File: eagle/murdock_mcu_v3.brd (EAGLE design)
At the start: 47 x 31.8 mm, 32 parts, among them IC1 MPU-9150, IC2 LT1763CS8-3.3, IC3 STM32F4XX_64, IC4 BMP085, Q2 PFET, U1 USD-SOCKETNEW, X1 USBSMD, X2 MURDOCK_STACK

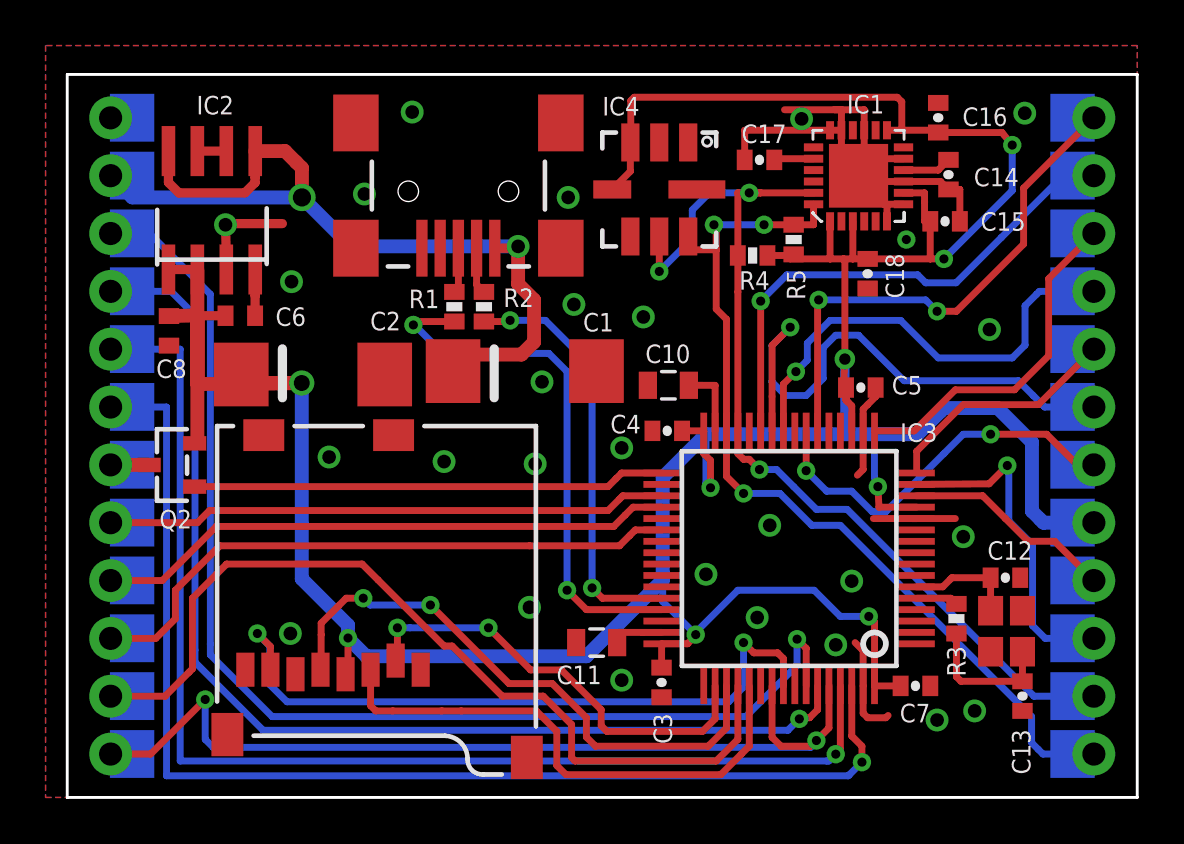
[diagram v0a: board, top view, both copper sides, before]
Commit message: usb placement & smaller tantal
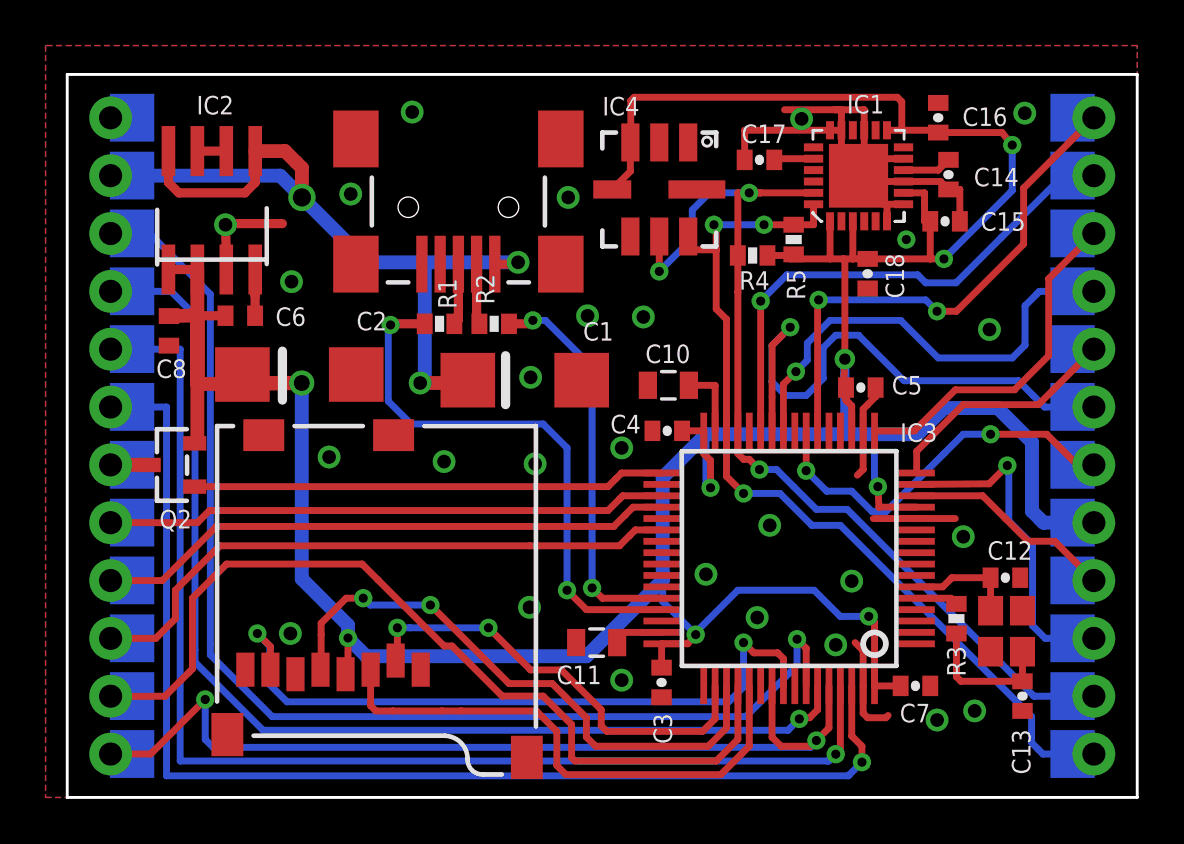
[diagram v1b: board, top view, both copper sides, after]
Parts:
- C1, C2: device rcl:SMC_D -> rcl:SMC_C
- moved R1 0.99 mm to (16.4, 20.8), turned to 0 degrees
- moved R2 0.87 mm to (18.8, 20.8), turned to 180 degrees
- moved X1 0.70 mm to (17.2, 25.9)
- moved C2 0.60 mm to (10.2, 18.6)
- moved C1 0.40 mm to (20.1, 18.3)
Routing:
- net A11: track 18.6 -> 17.5 mm
- net A12: track 23.6 -> 24.4 mm
- net +5V: track 39.4 -> 38.6 mm, vias 2 -> 3
- net N$2: track 1.99 -> 2.69 mm
- net N$1: track 2.05 -> 2.67 mm

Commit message: bootloader robustness
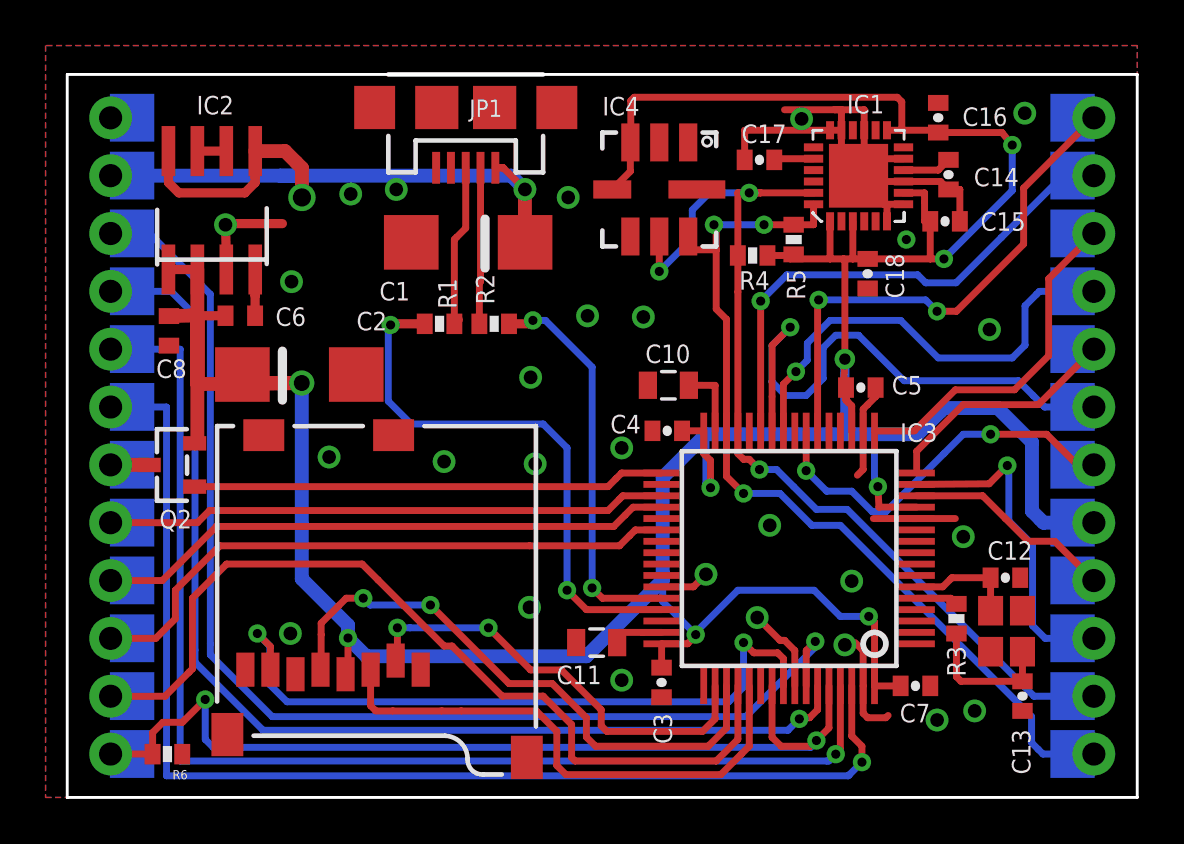
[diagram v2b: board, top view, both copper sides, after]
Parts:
- removed X1: USBSMD, SparkFun-Connectors:USB-MINIB
- added JP1: USB-MICROB, SparkFun-Connectors:USB-MICROB
- added R6: 15k, SparkFun:0402-RES
- moved C1 6.55 mm to (17.6, 24.4), turned to 180 degrees
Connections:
- net +5V: now also JP1.VBUS; no longer X1.VBUS
- net GND: now also IC3.43, IC3.57, JP1.GND, JP1.MT1, JP1.MT2, R6.1; no longer X1.GND
- net N$1: now also JP1.D-; no longer X1.D-
- net N$2: now also JP1.D+; no longer X1.D+
- net SW1: now also R6.2
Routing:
- net GND: track 45.0 -> 51.0 mm
- net N$2: track 2.69 -> 7.31 mm
- net N$1: track 2.67 -> 7.04 mm
- net +5V: track 38.6 -> 35.3 mm, vias 3 -> 2
- net SW1: track 41.1 -> 41.7 mm
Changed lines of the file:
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@@
 <wire x1="3.95" y1="23.615" x2="3.95" y2="23.405" width="0.2" layer="21"/>
 <wire x1="3.95" y1="23.615" x2="8.76" y2="23.625" width="0.2" layer="21"/>
-<wire x1="19.25" y1="17.25" x2="19.25" y2="19.4" width="0.4064" layer="21"/>
+<wire x1="18.35" y1="23.25" x2="18.35" y2="25.4" width="0.4064" layer="21"/>
 <wire x1="9.45" y1="17.45" x2="9.45" y2="19.6" width="0.4064" layer="21"/>
 <text x="18.35" y="18.9" size="1.4224" layer="22" font="vector" ratio="10" rot="MR0">MURDOCK</text>
@@
 <attribute name="VALUE" x="29.7975" y="6.6875" size="1.27" layer="27" rot="R90"/>
 </element>
-<element name="X1" library="SparkFun-Connectors" package="USB-MINIB" value="USBSMD" x="17.1775" y="25.92" smashed="yes" rot="R270">
-<attribute name="VALUE" x="17.1775" y="29.73" size="0.4064" layer="27" rot="R270"/>
-</element>
 <element name="U1" library="SparkFun-Connectors" package="MICRO-SD-SOCKET-PP" value="USD-SOCKETNEW" x="6.5825" y="16.31" smashed="yes" rot="R180">
 <attribute name="VALUE" x="15.4725" y="11.23" size="0.8128" layer="27" rot="R180"/>
@@
 <attribute name="VALUE" x="4.7725" y="19.155" size="0.6096" layer="27" font="vector" ratio="10" rot="R90"/>
 </element>
-<element name="C1" library="rcl" package="SMC_C" value="47µF/10V" x="20.0925" y="18.3225" smashed="yes">
-<attribute name="NAME" x="22.6525" y="20.0625" size="0.8128" layer="25" font="vector" ratio="10"/>
-<attribute name="VALUE" x="17.5525" y="14.5125" size="1.016" layer="27"/>
+<element name="C1" library="rcl" package="SMC_C" value="47µF/10V" x="17.6075" y="24.3775" smashed="yes" rot="R180">
+<attribute name="NAME" x="15.0475" y="22.6375" size="0.8128" layer="25" font="vector" ratio="10" rot="R180"/>
+<attribute name="VALUE" x="20.1475" y="28.1875" size="1.016" layer="27" rot="R180"/>
 </element>
 <element name="C2" library="rcl" package="SMC_C" value="100µF/6V" x="10.1925" y="18.5725" smashed="yes">
@@
 <element name="U$1" library="seb" package="C3D2_LOGO_SMALL" value="" x="17.1" y="22.55" rot="MR0"/>
 <element name="IC4" library="SparkFun-Sensors" package="BMP085" value="BMP085" x="26" y="26.7" smashed="yes" rot="R270"/>
+<element name="JP1" library="SparkFun-Connectors" package="USB-MICROB" value="USB-MICROB" x="17.5" y="30.3" rot="R180">
+<attribute name="PROD_ID" value="CONN-09505" x="17.5" y="30.3" size="1.778" layer="27" rot="R180" display="off"/>
+</element>
+<element name="R6" library="SparkFun" package="0402-RES" value="15k" x="4.4" y="1.9" rot="R180"/>
 </elements>
 <signals>
@@
 </polygon>
 <contactref element="X2" pad="GND"/>
-<contactref element="X1" pad="GND"/>
 <contactref element="U1" pad="GND1"/>
 <contactref element="U1" pad="GND3"/>
@@
 <via x="20.55" y="14.65" extent="1-16" drill="0.6"/>
 <via x="22.85" y="21.15" extent="1-16" drill="0.6"/>
-<via x="15.15" y="30.1" extent="1-16" drill="0.6"/>
+<via x="14.45" y="26.7" extent="1-16" drill="0.6"/>
 <via x="12.45" y="26.5" extent="1-16" drill="0.6"/>
 <via x="6.95" y="25.15" extent="1-16" drill="0.6"/>
@@
 <via x="24.35" y="5.15" extent="1-16" drill="0.6"/>
 <via x="30.3" y="7.9" extent="1-16" drill="0.6"/>
-<via x="33.75" y="6.7" extent="1-16" drill="0.6"/>
+<via x="34.15" y="6.7" extent="1-16" drill="0.6"/>
 <contactref element="IC1" pad="17"/>
 <contactref element="IC1" pad="18"/>
@@
 <via x="22" y="26.35" extent="1-16" drill="0.6"/>
 <contactref element="IC4" pad="1"/>
+<contactref element="JP1" pad="MT1"/>
+<contactref element="JP1" pad="MT2"/>
+<contactref element="JP1" pad="GND"/>
+<contactref element="IC3" pad="43"/>
+<contactref element="IC3" pad="57"/>
+<contactref element="R6" pad="1"/>
+<wire x1="26.1025" y1="9.2475" x2="27.4975" y2="9.2475" width="0.3048" layer="1"/>
+<wire x1="27.4975" y1="9.2475" x2="28.05" y2="9.8" width="0.3048" layer="1"/>
+<wire x1="31.9525" y1="4.8975" x2="31.9525" y2="6.4475" width="0.3048" layer="1"/>
+<wire x1="31.9525" y1="6.4475" x2="31.5" y2="6.9" width="0.3048" layer="1"/>
+<wire x1="31.5" y1="6.9" x2="31.3" y2="6.9" width="0.3048" layer="1"/>
+<wire x1="31.3" y1="6.9" x2="30.3" y2="7.9" width="0.3048" layer="1"/>
 </signal>
 <signal name="+3V3">
@@
 <wire x1="8.25" y1="27.23" x2="8.255" y2="28.385" width="0.4064" layer="1"/>
 <via x="10.3075" y="26.35" extent="1-16" drill="0.8"/>
-<contactref element="X1" pad="VBUS"/>
-<wire x1="18.7775" y1="23.42" x2="19.67" y2="23.42" width="0.4064" layer="1"/>
-<wire x1="19.67" y1="23.42" x2="19.8" y2="23.5" width="0.4064" layer="1"/>
-<via x="19.8" y="23.5" extent="1-16" drill="0.6"/>
-<wire x1="19.8" y1="23.5" x2="15.7" y2="23.5" width="0.6096" layer="16"/>
-<wire x1="15.7" y1="23.5" x2="13.1575" y2="23.5" width="0.6096" layer="16"/>
-<wire x1="13.1575" y1="23.5" x2="10.3075" y2="26.35" width="0.6096" layer="16"/>
+<via x="20.1" y="26.7" extent="1-16" drill="0.6"/>
 <wire x1="8.255" y1="28.385" x2="9.565" y2="28.385" width="0.6096" layer="1"/>
 <wire x1="9.565" y1="28.385" x2="10.05" y2="27.9" width="0.6096" layer="1"/>
 <wire x1="10.05" y1="27.9" x2="10.3075" y2="27.6425" width="0.6096" layer="1"/>
 <wire x1="10.3075" y1="27.6425" x2="10.3075" y2="26.35" width="0.6096" layer="1"/>
-<wire x1="10.3075" y1="26.35" x2="9.3525" y2="27.305" width="0.6096" layer="16"/>
 <wire x1="9.3525" y1="27.305" x2="1.905" y2="27.305" width="0.6096" layer="16"/>
-<wire x1="17.5925" y1="18.3225" x2="17.47" y2="18.2" width="0.6096" layer="1"/>
-<wire x1="17.47" y1="18.2" x2="15.5" y2="18.2" width="0.6096" layer="1"/>
-<via x="15.5" y="18.2" extent="1-16" drill="0.6"/>
-<wire x1="15.5" y1="18.2" x2="15.7" y2="18.4" width="0.6096" layer="16"/>
-<wire x1="15.7" y1="18.4" x2="15.7" y2="23.5" width="0.6096" layer="16"/>
+<contactref element="JP1" pad="VBUS"/>
+<wire x1="18.8" y1="27.65" x2="19.15" y2="27.65" width="0.3048" layer="1"/>
+<wire x1="20.1" y1="26.7" x2="19.15" y2="27.65" width="0.3048" layer="1"/>
+<wire x1="19.15" y1="27.65" x2="18.8" y2="27.65" width="0.3048" layer="1"/>
+<wire x1="20.1075" y1="24.3775" x2="20.1" y2="24.385" width="0.6096" layer="1"/>
+<wire x1="20.1" y1="24.385" x2="20.1" y2="26.7" width="0.6096" layer="1"/>
+<wire x1="9.3525" y1="27.305" x2="19.495" y2="27.305" width="0.6096" layer="16"/>
+<wire x1="19.495" y1="27.305" x2="20.1" y2="26.7" width="0.6096" layer="16"/>
+<wire x1="9.3525" y1="27.305" x2="10.3075" y2="27.305" width="0.6096" layer="16"/>
+<wire x1="10.3075" y1="27.305" x2="10.3075" y2="26.35" width="0.6096" layer="16"/>
 </signal>
 <signal name="N$13">
@@
 <contactref element="X2" pad="PWM1"/>
 <contactref element="IC3" pad="58"/>
-<wire x1="32.4525" y1="4.8975" x2="32.4525" y2="6.5475" width="0.3048" layer="1"/>
-<wire x1="32.4525" y1="6.5475" x2="32.05" y2="6.95" width="0.3048" layer="1"/>
-<via x="32.05" y="6.95" extent="1-16" drill="0.4"/>
-<wire x1="32.05" y1="6.95" x2="32.05" y2="5.8" width="0.3048" layer="16"/>
-<wire x1="32.05" y1="5.8" x2="29.8" y2="3.55" width="0.3048" layer="16"/>
+<wire x1="32.4525" y1="4.8975" x2="32.4525" y2="6.4475" width="0.3048" layer="1"/>
+<wire x1="32.4525" y1="6.4475" x2="32.85" y2="6.85" width="0.3048" layer="1"/>
+<via x="32.85" y="6.85" extent="1-16" drill="0.4"/>
+<wire x1="32.85" y1="6.85" x2="32.85" y2="6.6" width="0.3048" layer="16"/>
+<wire x1="32.85" y1="6.6" x2="29.8" y2="3.55" width="0.3048" layer="16"/>
 <wire x1="29.8" y1="3.55" x2="9" y2="3.55" width="0.3048" layer="16"/>
 <wire x1="6.285" y1="6.7476" x2="6.285" y2="22.0976" width="0.3048" layer="16"/>
@@
 </signal>
 <signal name="N$1">
-<contactref element="X1" pad="D-"/>
 <contactref element="R2" pad="2"/>
 <wire x1="18.1" y1="20.8" x2="17.9775" y2="20.9225" width="0.4064" layer="1"/>
-<wire x1="17.9775" y1="20.9225" x2="17.9775" y2="23.42" width="0.4064" layer="1"/>
+<contactref element="JP1" pad="D-"/>
+<wire x1="18.15" y1="27.65" x2="18.15" y2="22.65" width="0.3048" layer="1"/>
+<wire x1="18.15" y1="22.65" x2="18.1" y2="22.6" width="0.3048" layer="1"/>
+<wire x1="18.1" y1="22.6" x2="18.1" y2="20.8" width="0.3048" layer="1"/>
 </signal>
 <signal name="N$2">
-<contactref element="X1" pad="D+"/>
 <contactref element="R1" pad="2"/>
-<wire x1="17.1775" y1="23.42" x2="17.1775" y2="20.9775" width="0.4064" layer="1"/>
 <wire x1="17.1775" y1="20.9775" x2="17" y2="20.8" width="0.4064" layer="1"/>
+<contactref element="JP1" pad="D+"/>
+<wire x1="17.5" y1="27.65" x2="17.5" y2="25" width="0.3048" layer="1"/>
+<wire x1="17.5" y1="25" x2="17.1" y2="24.6" width="0.3048" layer="1"/>
+<wire x1="17.1" y1="24.6" x2="17" y2="24.5" width="0.3048" layer="1"/>
+<wire x1="17" y1="24.5" x2="17" y2="20.8" width="0.3048" layer="1"/>
 </signal>
 <signal name="A11">
@@
 <wire x1="31.349071875" y1="2.247578125" x2="32.647578125" y2="2.247578125" width="0.3048" layer="1"/>
 <wire x1="32.647578125" y1="2.247578125" x2="32.9" y2="2.5" width="0.3048" layer="1"/>
-<wire x1="1.905" y1="1.905" x2="3.6628" y2="1.905" width="0.3048" layer="1"/>
-<wire x1="3.6628" y1="1.905" x2="6.0596" y2="4.3018" width="0.3048" layer="1"/>
+<contactref element="R6" pad="2"/>
+<wire x1="1.905" y1="1.905" x2="3.75" y2="1.905" width="0.3048" layer="1"/>
+<wire x1="3.75" y1="1.905" x2="3.75" y2="1.9" width="0.3048" layer="1"/>
+<wire x1="3.75" y1="1.9" x2="3.75" y2="2.85" width="0.3048" layer="1"/>
+<wire x1="3.75" y1="2.85" x2="4.2" y2="3.3" width="0.3048" layer="1"/>
+<wire x1="4.2" y1="3.3" x2="5.0578" y2="3.3" width="0.3048" layer="1"/>
+<wire x1="5.0578" y1="3.3" x2="6.0596" y2="4.3018" width="0.3048" layer="1"/>
 </signal>
 <signal name="SDA">

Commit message: pwm/sbus to new pin @usart2 & led_l moved
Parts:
- renumbered Q2 to T1
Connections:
- net LED_L: now also IC3.20; no longer IC3.17
- net PWM2: now also IC3.17; no longer IC3.59
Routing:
- net PWM2: track 49.4 -> 69.2 mm
- net LED_L: track 15.2 -> 19.5 mm, vias 0 -> 2
- net +3V3: track 171.7 -> 174.3 mm
- net LED_C: track 20.3 -> 19.1 mm
- net GND: track 51.0 -> 51.9 mm, vias 27 -> 29

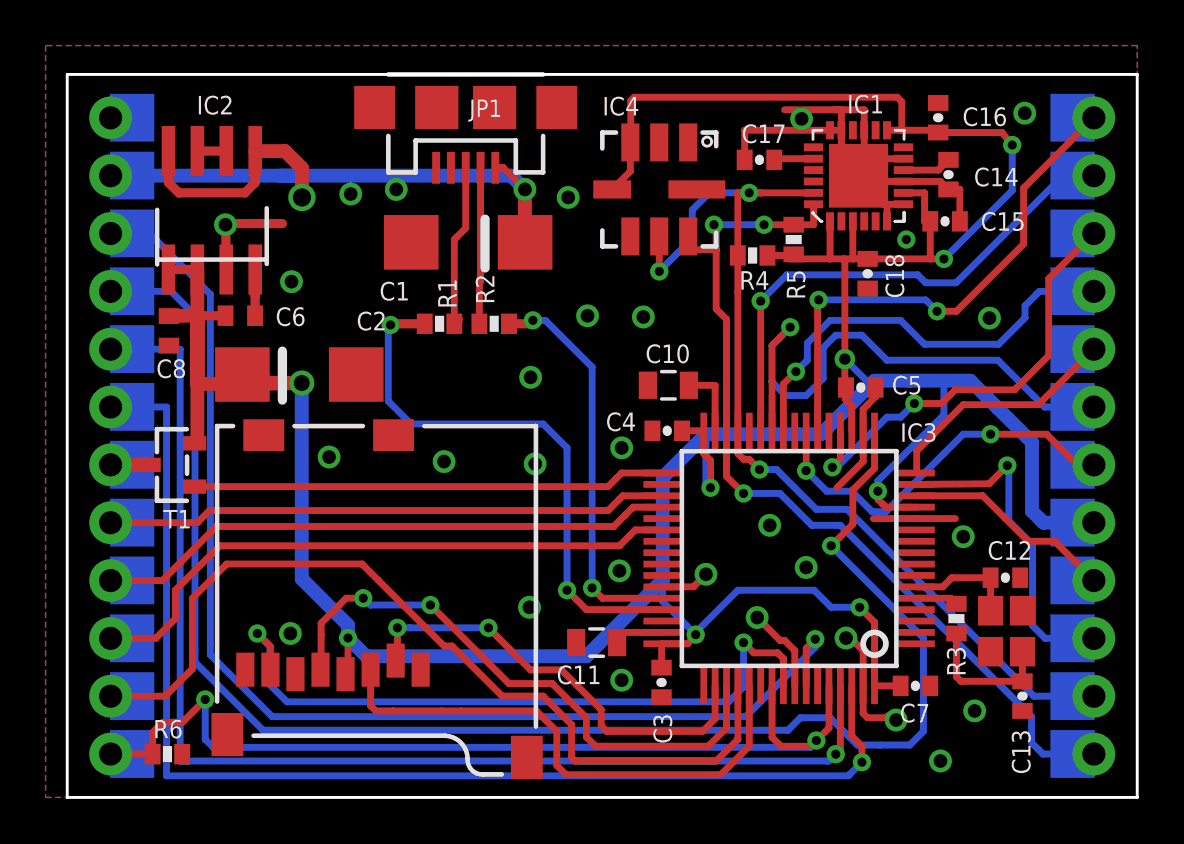
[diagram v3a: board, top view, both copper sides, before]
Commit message: added eeprom
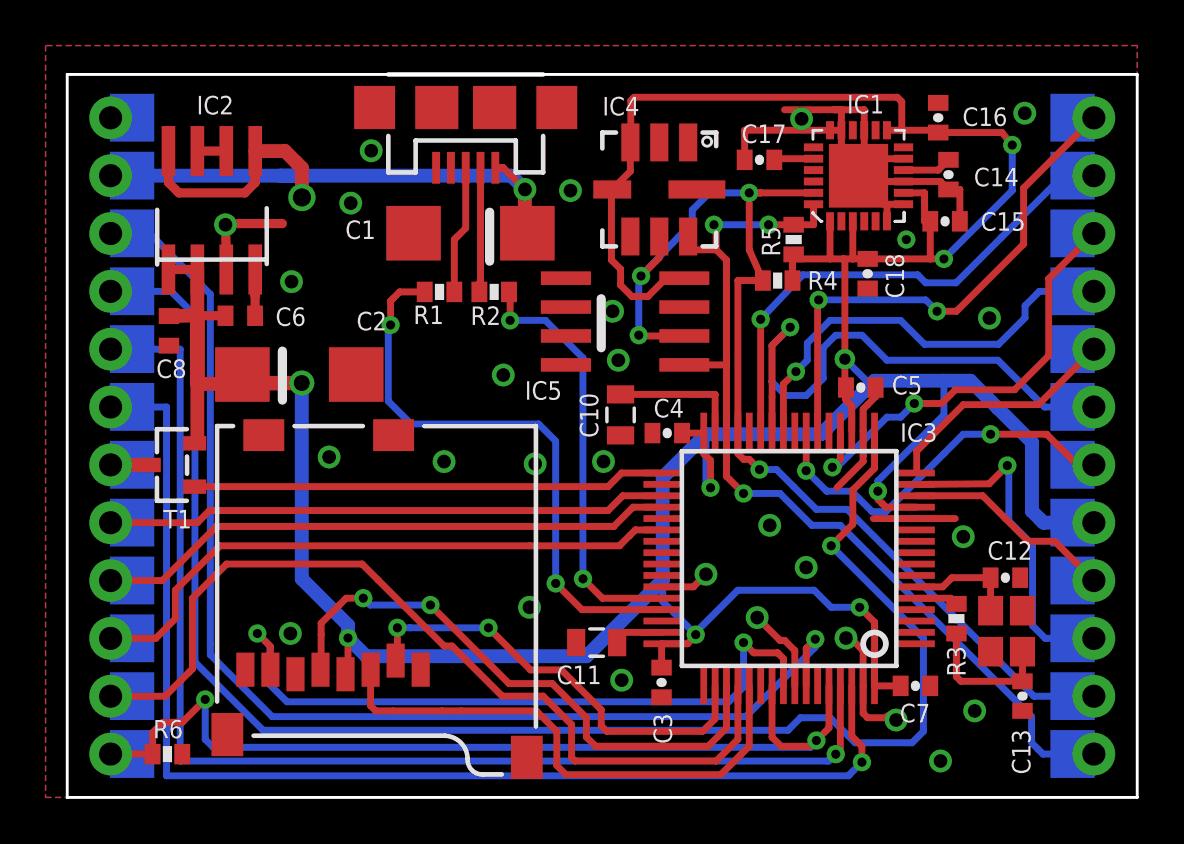
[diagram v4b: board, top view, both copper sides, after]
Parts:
- added IC5: 24LC16BSN, microchip:SO-08
- moved C10 2.47 mm to (24.3, 16.8), turned to 90 degrees
- moved R4 1.56 mm to (31.2, 22.7)
- moved R1 1.40 mm to (16.4, 22.2)
- moved R2 1.40 mm to (18.8, 22.2)
- moved C1 0.41 mm to (17.7, 24.8)
- moved C4 0.10 mm to (26.4, 16.0)
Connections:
- net +3V3: now also IC5.8
- net GND: now also IC5.1, IC5.2, IC5.3, IC5.4
- net SCL: now also IC5.6
- net SDA: now also IC5.5
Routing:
- net +3V3: track 174.3 -> 182.1 mm
- net SCL: track 43.0 -> 49.4 mm, vias 3 -> 4
- net N$3: track 3.15 -> 5.75 mm
- net SDA: track 40.1 -> 42.2 mm
- net N$2: track 7.31 -> 5.78 mm
- net N$1: track 7.04 -> 5.62 mm
- net A12: track 24.4 -> 25.6 mm
- net A11: track 17.5 -> 18.7 mm
- net GND: vias 29 -> 28
